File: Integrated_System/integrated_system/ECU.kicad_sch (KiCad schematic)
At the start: 38 parts, among them J1 Jack-DC, J2 Fan 1, J3 Fan 2, J4 Fan 3, Q2 TN0702N3, Q3 TN0702N3, Q4 TN0702N3, U1 DC to DC Buck Converter 12V t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, U2 BME680, U5 SGP30, U7 SCD30

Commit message: changed ground
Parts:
- renumbered A1 to A?, C1 to C?, C2 to C?, D5 to D?, D9 to D?, D1 to D?, D8 to D?, D3 to D?, D6 to D?, D10 to D?, D2 to D?, D7 to D?, D4 to D?, D11 to D?, J4 to J?, J2 to J?, J1 to J?, J3 to J?, ON/OFF_SWITCH to ON/OFF_SWITCH?, Q2 to Q?, Q4 to Q?, Q3 to Q?, R1 to R?, R14 to R?, R4 to R?, R10 to R?, R2 to R?, R13 to R?, R6 to R?, R11 to R?, R12 to R?, R5 to R?, R3 to R?, RV1 to RV?, U7 to U?, U1 to U?, U5 to U?, U2 to U?

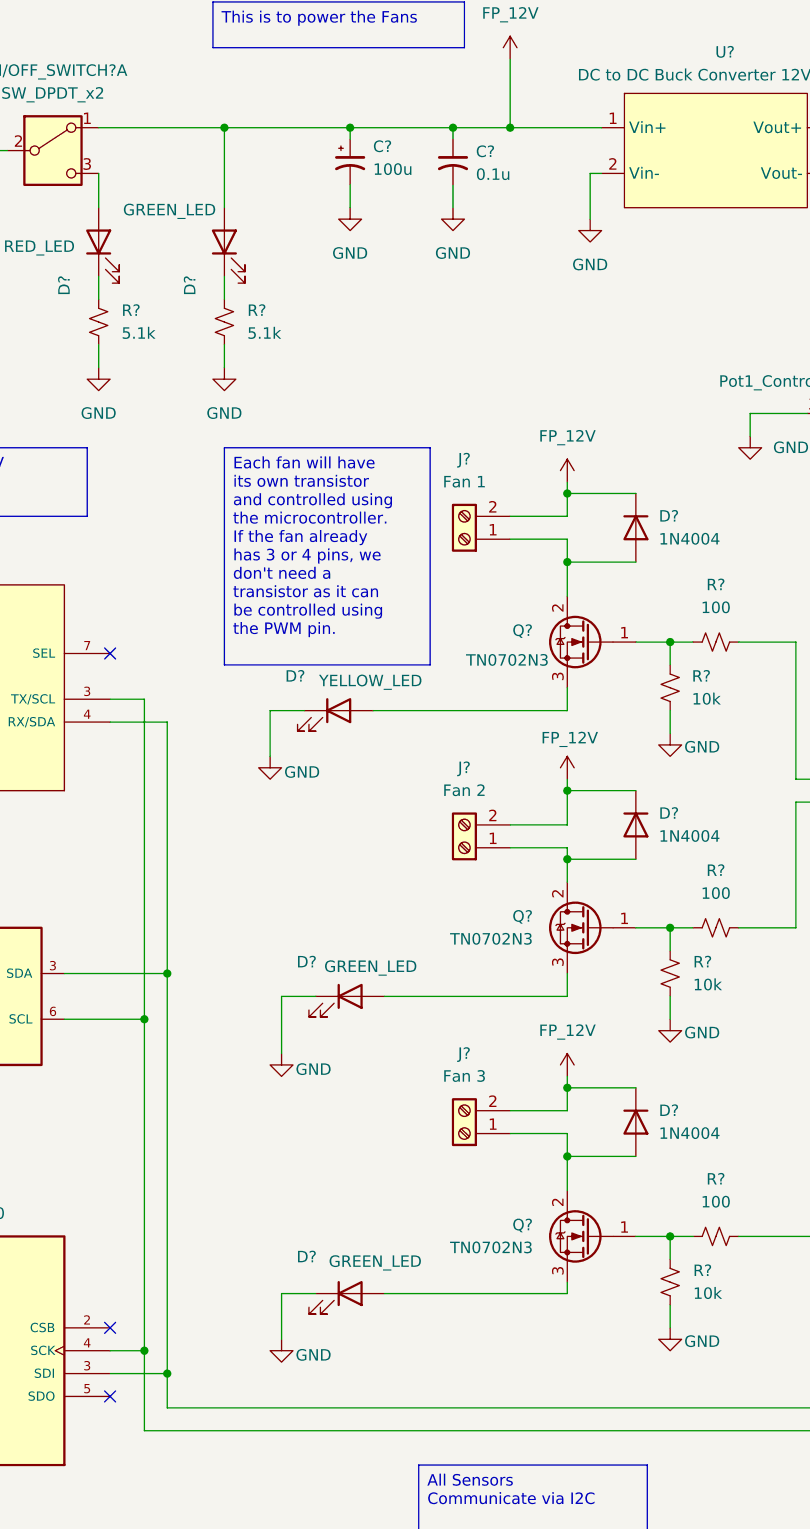
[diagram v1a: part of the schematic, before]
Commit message: Updated LED schematic
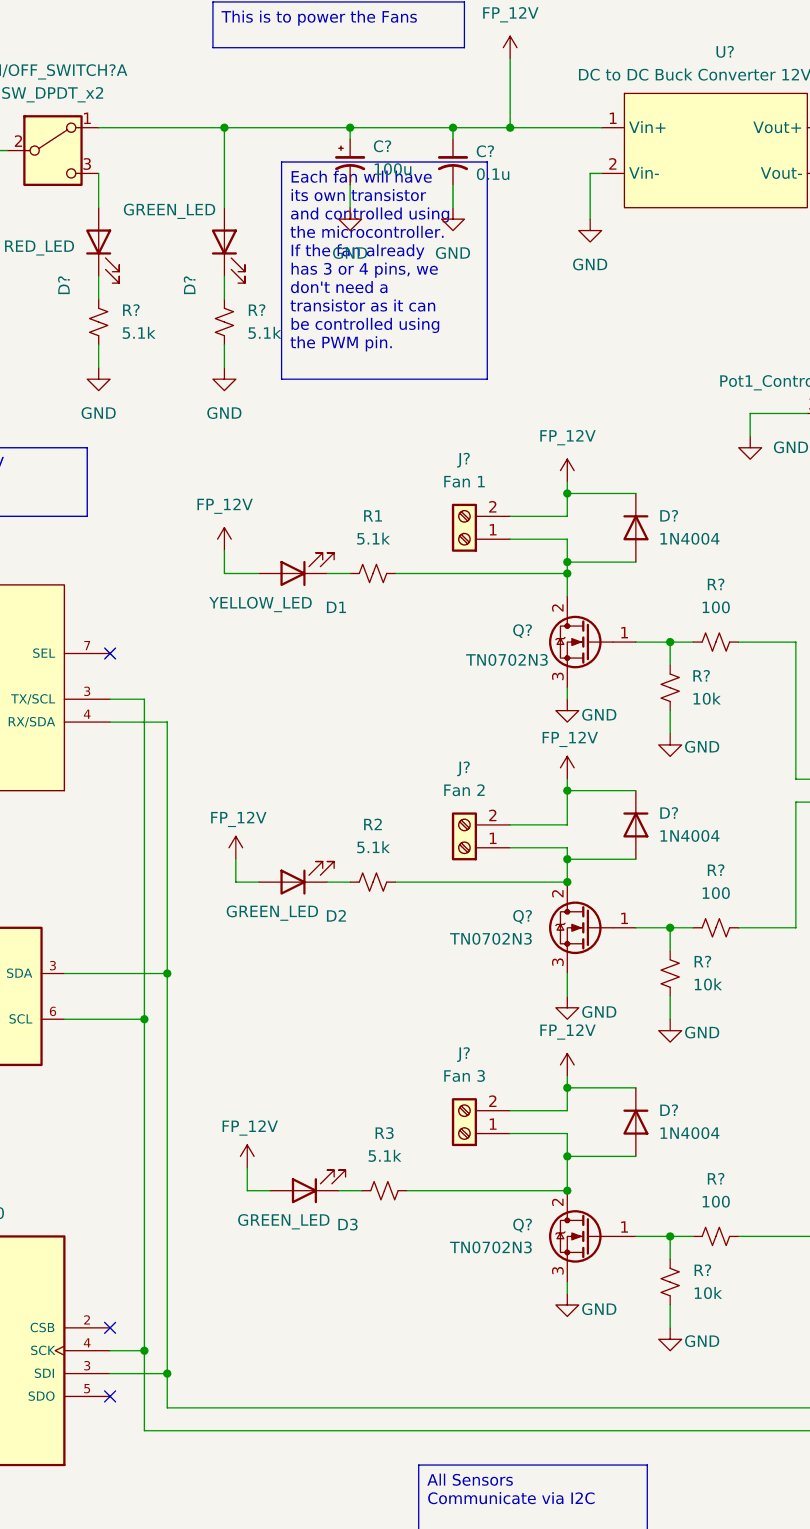
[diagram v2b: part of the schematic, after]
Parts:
- removed D? (x2): GREEN_LED, symbol Device:LED
- removed D?: YELLOW_LED, symbol Device:LED
- added D1: YELLOW_LED, symbol Device:LED
- added D2, D3: GREEN_LED, symbol Device:LED
- added R1, R2, R3: 5.1k, symbol Device:R_Small_US
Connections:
- net FP_12V: now also D1.2 (A), D2.2 (A), D3.2 (A)
- net GND: now also Q?.3 (S), Q?.3 (S), Q?.3 (S)
- net at D?.2 (A), J?.1 (Pin_1), Q?.2 (D): now also R3.2
- net at D?.2 (A), J?.1 (Pin_1), Q?.2 (D): now also R1.2
- net at D?.2 (A), J?.1 (Pin_1), Q?.2 (D): now also R2.2
- new net: D1.1 (K), R1.1
- new net: D2.1 (K), R2.1
- new net: D3.1 (K), R3.1

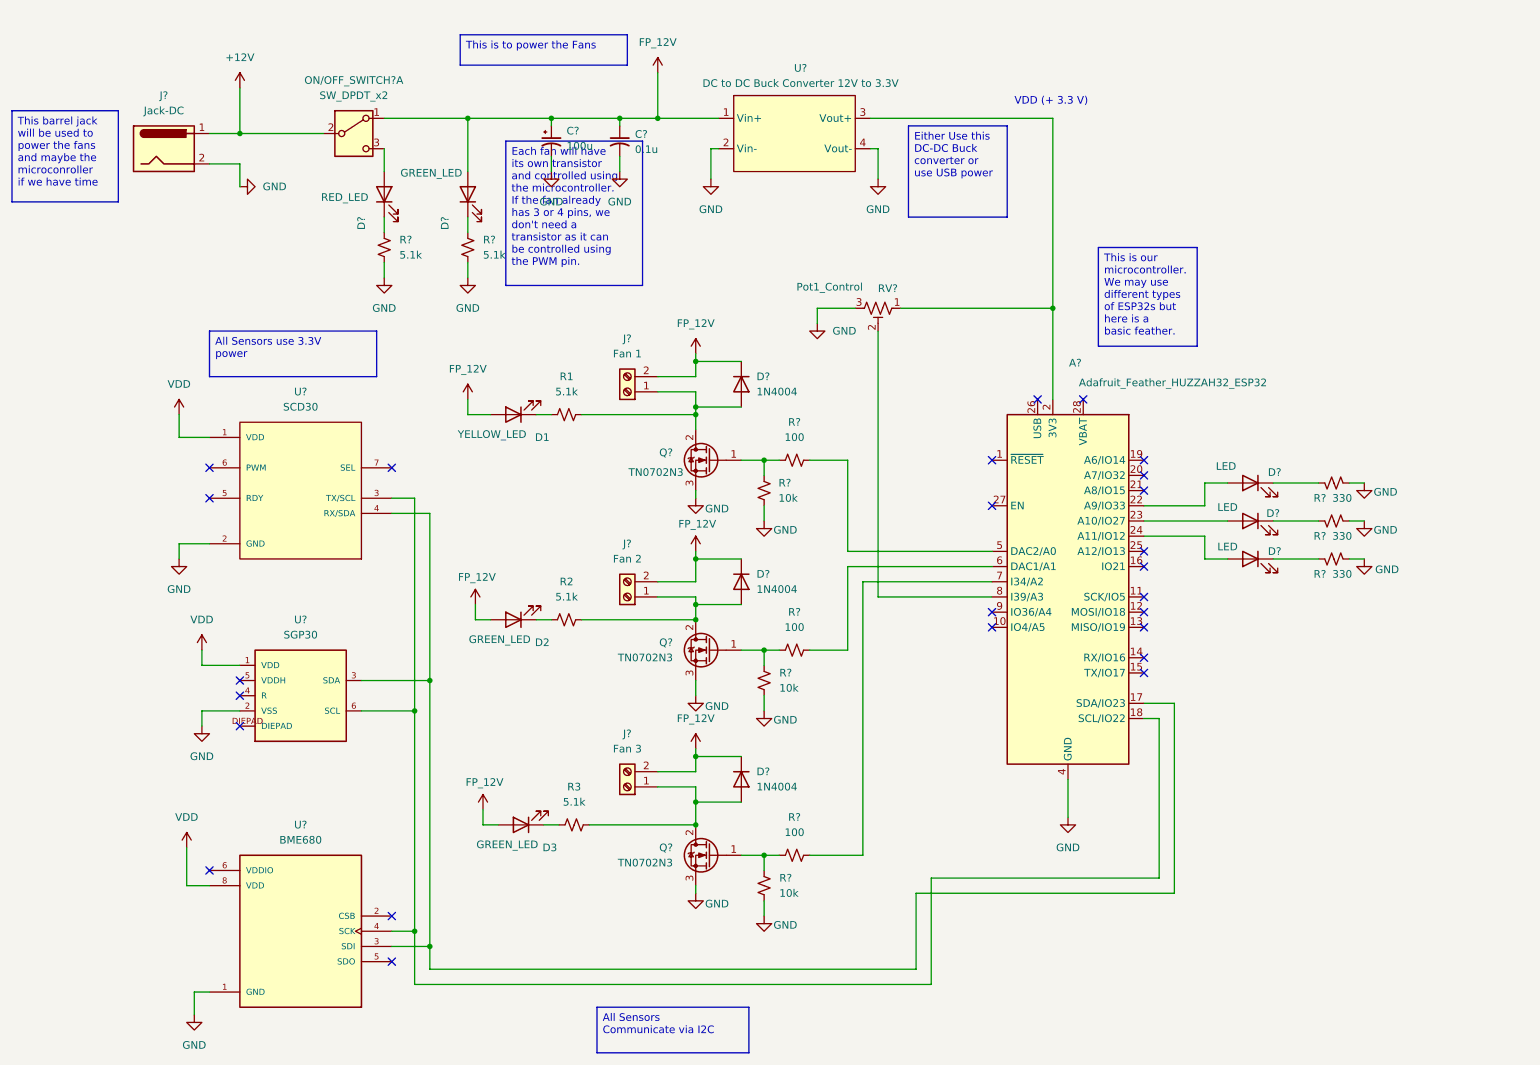
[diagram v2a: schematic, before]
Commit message: Updated the descriptions
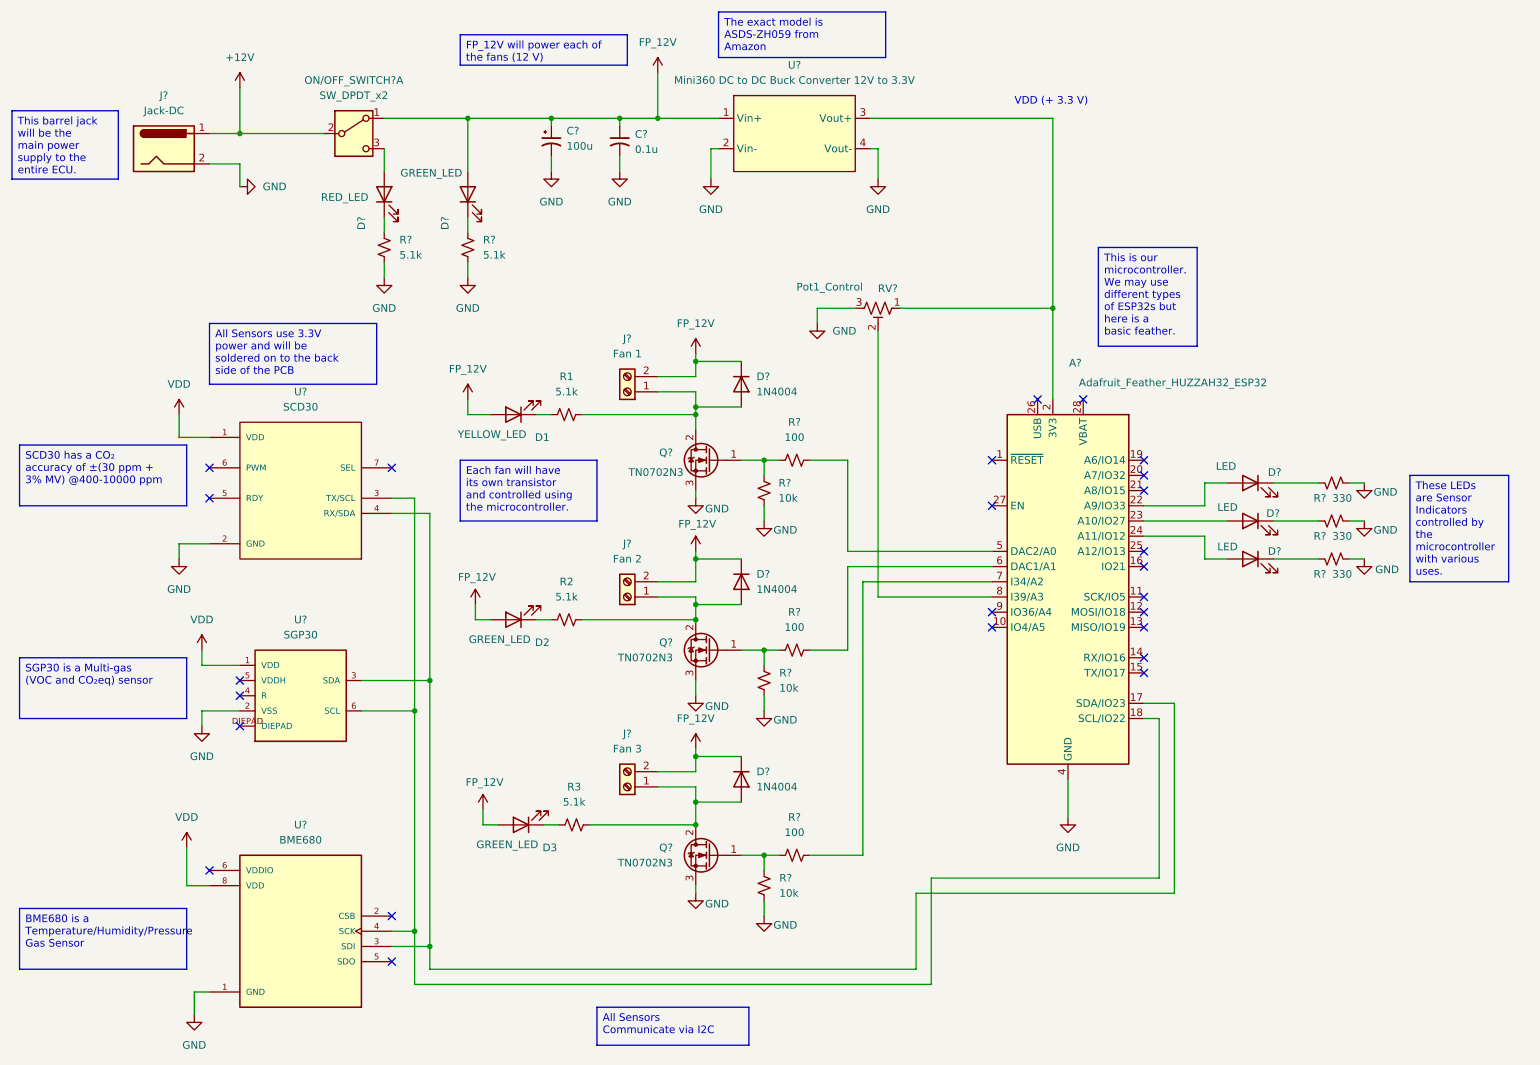
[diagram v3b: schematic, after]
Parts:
- U?: value DC to DC Buck Converter 12V to 3.3V -> Mini360 DC to DC Buck Converter 12V to 3.3V
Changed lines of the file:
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@@
 	(title_block
 		(title "Integrated System")
-		(date "2026-04-14")
-		(rev "1.1")
+		(date "2026-04-20")
+		(rev "1.2")
 		(company "OSSEM")
 	)
@@
 		)
 	)
-	(text_box "Either Use this DC-DC Buck converter or use USB power"
+	(text_box "These LEDs are Sensor Indicators controlled by the microcontroller with various uses."
 		(exclude_from_sim no)
-		(at 162.56 33.02 0)
-		(size 16.51 15.24)
+		(at 246.38 91.44 0)
+		(size 16.51 17.78)
 		(margins 0.9525 0.9525 0.9525 0.9525)
 		(stroke
@@
 		)
 	)
-	(text_box "Each fan will have its own transistor and controlled using the microcontroller. If the fan already has 3 or 4 pins, we don't need a transistor as it can be controlled using the PWM pin."
+	(text_box "Each fan will have its own transistor and controlled using the microcontroller."
 		(exclude_from_sim no)
-		(at 95.25 35.56 0)
-		(size 22.86 24.13)
+		(at 87.63 88.9 0)
+		(size 22.86 10.16)
 		(margins 0.9525 0.9525 0.9525 0.9525)
 		(stroke
@@
 		)
 	)
-	(text_box "This is to power the Fans"
+	(text_box "BME680 is a Temperature/Humidity/Pressure Gas Sensor"
+		(exclude_from_sim no)
+		(at 13.97 163.83 0)
+		(size 27.94 10.16)
+		(margins 0.9525 0.9525 0.9525 0.9525)
+		(stroke
+			(width 0)
+			(type solid)
+		)
+		(fill
+			(type none)
+		)
+		(effects
+			(font
+				(size 1.27 1.27)
+			)
+			(justify left top)
+		)
+	)
+	(text_box "SGP30 is a Multi-gas (VOC and CO₂eq) sensor"
+		(exclude_from_sim no)
+		(at 13.97 121.92 0)
+		(size 27.94 10.16)
+		(margins 0.9525 0.9525 0.9525 0.9525)
+		(stroke
+			(width 0)
+			(type solid)
+		)
+		(fill
+			(type none)
+		)
+		(effects
+			(font
+				(size 1.27 1.27)
+			)
+			(justify left top)
+		)
+	)
+	(text_box "FP_12V will power each of the fans (12 V)"
 		(exclude_from_sim no)
 		(at 87.63 17.78 0)
@@
 		)
 	)
-	(text_box "All Sensors use 3.3V power"
+	(text_box "The exact model is ASDS-ZH059 from Amazon"
 		(exclude_from_sim no)
-		(at 45.72 67.31 0)
+		(at 130.81 13.97 0)
 		(size 27.94 7.62)
 		(margins 0.9525 0.9525 0.9525 0.9525)
@@
 		)
 	)
+	(text_box "All Sensors use 3.3V power and will be soldered on to the back side of the PCB"
+		(exclude_from_sim no)
+		(at 45.72 66.04 0)
+		(size 27.94 10.16)
+		(margins 0.9525 0.9525 0.9525 0.9525)
+		(stroke
+			(width 0)
+			(type solid)
+		)
+		(fill
+			(type none)
+		)
+		(effects
+			(font
+				(size 1.27 1.27)
+			)
+			(justify left top)
+		)
+	)
 	(text_box "All Sensors Communicate via I2C"
 		(exclude_from_sim no)
 		(at 110.49 180.34 0)
-		(size 25.4 7.62)
+		(size 25.4 6.35)
+		(margins 0.9525 0.9525 0.9525 0.9525)
+		(stroke
+			(width 0)
+			(type solid)
+		)
+		(fill
+			(type none)
+		)
+		(effects
+			(font
+				(size 1.27 1.27)
+			)
+			(justify left top)
+		)
+	)
+	(text_box "SCD30 has a CO₂ accuracy of ±(30 ppm + 3% MV) @400-10000 ppm"
+		(exclude_from_sim no)
+		(at 13.97 86.36 0)
+		(size 27.94 10.16)
 		(margins 0.9525 0.9525 0.9525 0.9525)
 		(stroke
@@
 		)
 	)
-	(text_box "This barrel jack will be used to power the fans and maybe the microconroller if we have time"
+	(text_box "This barrel jack will be the main power supply to the entire ECU."
 		(exclude_from_sim no)
 		(at 12.7 30.48 0)
-		(size 17.78 15.24)
+		(size 17.78 11.43)
 		(margins 0.9525 0.9525 0.9525 0.9525)
 		(stroke
@@
 		(fields_autoplaced yes)
 		(property "Reference" "U?"
-			(at 144.526 23.368 0)
+			(at 143.51 22.86 0)
 			(effects
 				(font
@@
 			)
 		)
-		(property "Value" "DC to DC Buck Converter 12V to 3.3V"
-			(at 144.526 25.908 0)
+		(property "Value" "Mini360 DC to DC Buck Converter 12V to 3.3V"
+			(at 143.51 25.4 0)
 			(effects
 				(font
